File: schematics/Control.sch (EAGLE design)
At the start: 57 parts, among them IC1 THAT1646, IC2 THAT1646, IC5 NE5532N

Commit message: rev01 for pcbtrain express fab
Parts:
- removed BOOT, BOOT1, JP4: (no value), SparkFun:M03PTH
- removed C501, C502: 2n7 C0G, Rebel:C-EUC0603
- removed C503, C504: 100n, Rebel:C-EUC0603
- removed JP2: (no value), SparkFun:M02PTH
- added C10, C300, C301, C9: 0.1uF, capacitor-wima:C5/3.5
- added C11, C12, C610: 100n, rcl:C-EU050-025X075
- added C13, C14: 2n7 C0G, rcl:C-EU050-025X075
- added C15, C16, C611: 100uF, rcl:CPOL-EUE2.5-7
- added IN2: (no value), SparkFun:M02PTH
- added J4, J5: NEUTRIK_NMJ6HCD2, neutrik_jacks:NEUTRIK_NMJ6HCD2
- added JP13: (no value), SparkFun:M05PTH
- added R1, R2, R3, R4, R5: 91R, Rebel:R-EU_0204/7
- added R300, R301: 2M, Rebel:R-EU_0204/7
- added UART: (no value), SparkFun:M03PTH
- JP1: device SparkFun:M02PTH -> SparkFun:M05PTH
- R501, R502, R503, R504, R505, R506, R507, R508, R509, R510: device Rebel:R-EU_0603 -> Rebel:R-EU_0204/7
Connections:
- removed net +3V3: BOOT.3, BOOT1.3, JP3.3, JP4.3, JP5.3
- removed net AINA: C501.1, R503.2
- removed net AINB: C502.1, R508.2
- removed net BOOT0: BOOT.2, BOOT1.2, JP12.2, JP9.2
- removed net INL: R502.1
- removed net INR: R507.1
- removed net L_IN1: IN.1
- removed net L_IN2: IN1.1
- removed net L_OUT1: HP.2
- removed net L_OUT2: HP1.2
- removed net OUT_LEFT: IC1.4
- removed net OUT_RIGHT: IC2.4
- removed net R_IN1: IN.2
- removed net R_IN2: IN1.2
- removed net R_OUT1: HP.1
- removed net R_OUT2: HP1.1
- removed net USB_VBUS: JP1.2, JP2.2, USB.4, USB1.4
- new net ADC1_A: ADC.4
- new net ADC2_A: ADC.3
- new net ADC3_A: ADC.2
- new net ADC4_A: ADC.1
- new net FX_IN_L: C300.2, J4.T, J5.TN, R300.2
- new net FX_IN_R: C301.2, J5.T, R301.2
- new net L_IN_A: IN.1, R1.1
- new net L_IN_B: C13.1, IN1.1, R503.2
- new net L_OUT_A: C10.2, HP.2
- new net L_OUT_B: HP1.2, R1.2
- new net N$26: C300.1, R502.1
- new net N$30: C301.1, R507.1
- new net N$7: C9.1, IC2.4
- new net N$9: C10.1, IC1.4
- new net PA2_A: JP7.2
- new net PA3_A: JP7.1
- new net PB6_A: JP9.4
- new net PB7_A: JP9.3
- new net PE2_A: JP10.4
- new net PE3_A: JP10.3
- new net PE4_A: JP10.2
- new net PE5_A: JP10.1
- new net PG14_A: JP9.1
- new net RX: R3.1, UART.3
- new net RX_A: JP13.2, R5.1
- new net RX_B: JP1.2, R3.2
- new net R_IN_A: IN.2, R2.1
- new net R_IN_B: C14.1, IN1.2, R508.2
- new net R_OUT_A: C9.2, HP.1
- new net R_OUT_B: HP1.1, R2.2
- new net TX: R4.1, UART.1
- new net TX_A: JP13.3, R4.2
- new net TX_B: JP1.3, R5.2
- new net USB_DM_A: USB.3
- new net USB_DP_A: USB.2
- new net USB_ID_A: USB.1
- net +12V: now also C11.1; no longer C503.1
- net +5V: now also C15.+, C16.+; no longer JP1.1, JP2.1, JP4.1
- net -12V: now also C12.1; no longer C504.1
- net ADC1: no longer ADC.4
- net ADC2: no longer ADC.3
- net ADC3: no longer ADC.2
- net ADC4: no longer ADC.1
- net CS_VREF: now also C13.2, C14.2, C610.1, C611.+, VMID1.1; no longer C501.2, C502.2
- net GND: now also C11.2, C12.2, C15.-, C16.-, C610.2, C611.-, IN2.2, J4.S, J4.TN, J5.S, JP12.2, JP9.2, R300.1, R301.1, UART.2; no longer BOOT.1, BOOT1.1, C503.2, C504.2, JP4.2
- net GNDA: now also IN2.1
- net PA2: no longer JP7.2
- net PA3: no longer JP7.1
- net PB6: no longer JP9.4
- net PB7: no longer JP9.3
- net PE2: no longer JP10.4
- net PE3: no longer JP10.3
- net PE4: no longer JP10.2
- net PE5: no longer JP10.1
- net PG14: no longer JP9.1
- net USB_DM: no longer USB.3
- net USB_DP: no longer USB.2
- net USB_ID: no longer USB.1
- net VCC/2: no longer VMID1.1
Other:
- note added: "Copyright 2016 Rebel Technology"
- note added: "OWL Rack Revision 1"
- note removed: "Copyright 2015 Rebel Technology"
- note removed: "OWL Modular Revision 2"
- moved on the sheet: C1, C2, C3, C4, C5, C6, C7, C8, IC1, IC2, LEFT, RIGHT

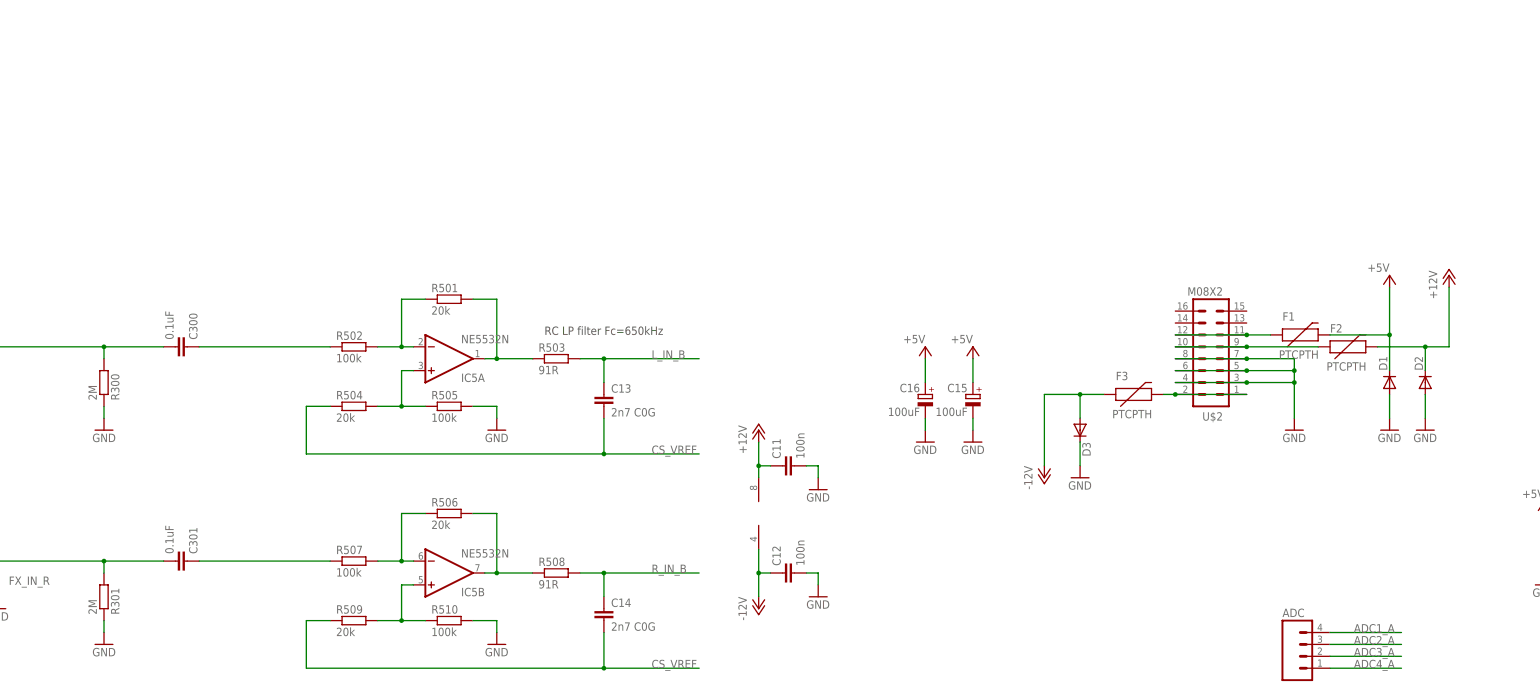
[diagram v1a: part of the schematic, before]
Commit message: added +5v reg, change power connection, reduced board size
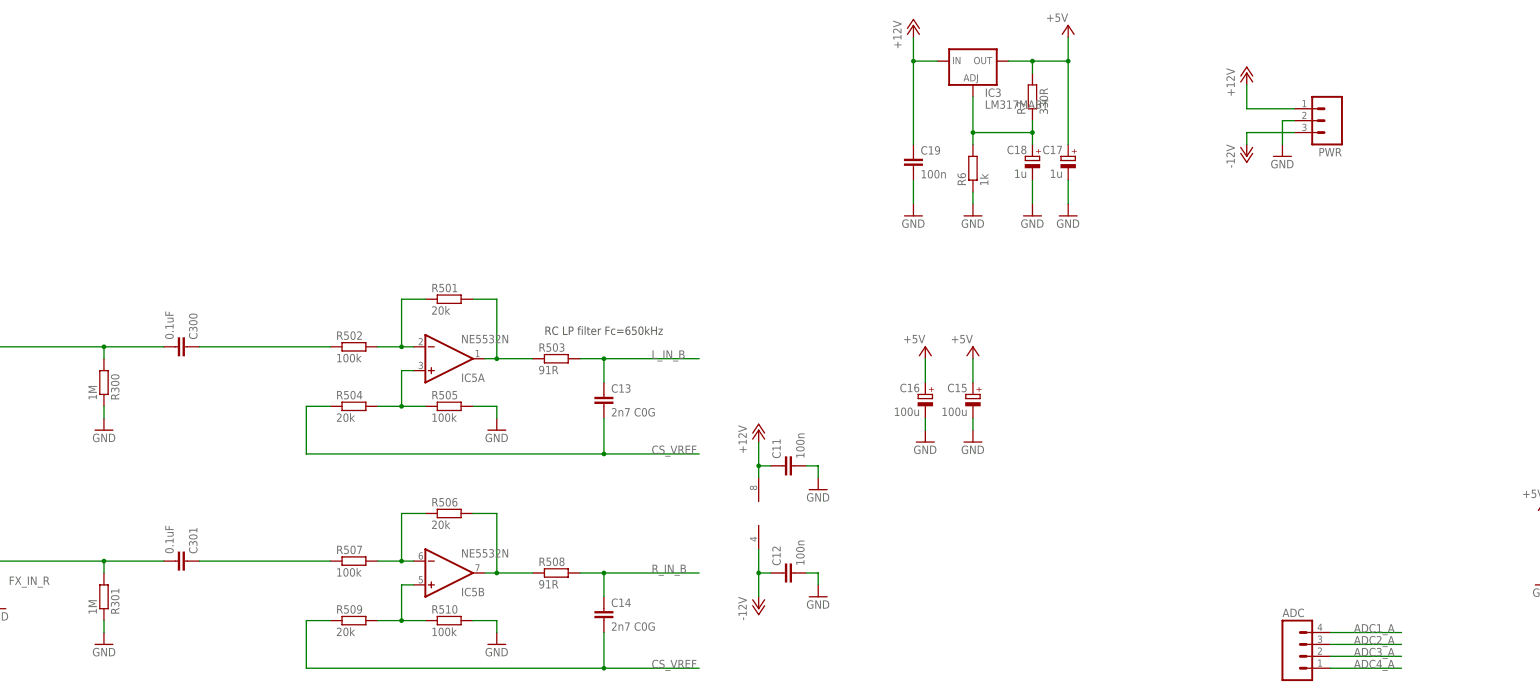
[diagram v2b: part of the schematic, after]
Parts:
- removed D1, D2, D3: (no value), Rebel:DIODE1N4001
- removed F1, F2, F3: PTCPTH, Rebel:PTCPTH
- removed U$2: M08X2, SparkFun:M08X2
- added C17, C18: 1u, rcl:CPOL-EUE2.5-7
- added C19: 100n, rcl:C-EU050-025X075
- added IC3: LM317MABT, v-reg:LM317MABT
- added PWR: (no value), SparkFun:M03PTH
- added R6: 1k, Rebel:R-EU_0204/7
- added R7: 330R, Rebel:R-EU_0204/7
- C15, C16: value 100uF -> 100u
- R300, R301: value 2M -> 1M
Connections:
- removed net N$44: F1.1, U$2.11, U$2.12
- removed net N$45: F2.1, U$2.10, U$2.9
- removed net N$6: F3.2, U$2.1, U$2.2
- new net N$11: C18.+, IC3.ADJ, R6.2, R7.1
- net +12V: now also C19.1, IC3.IN, PWR.1; no longer D2.C, F2.2
- net +5V: now also C17.+, IC3.OUT, R7.2; no longer D1.C, F1.2
- net -12V: now also PWR.3; no longer D3.A, F3.1
- net GND: now also C17.-, C18.-, C19.2, PWR.2, R6.1; no longer D1.A, D2.A, D3.C, U$2.3, U$2.4, U$2.5, U$2.6, U$2.7, U$2.8

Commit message: added usb connections and adjusted audio input circuit
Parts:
- added R8, R9: 1M, Rebel:R-EU_0204/7
- added USBA, USBB: (no value), SparkFun:M03PTH
- R501, R504, R506, R509: value 20k -> 10k
- R502, R505, R507, R510: value 100k -> 10k
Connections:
- net USB_ID renamed USB_ID_B
- removed net USB_DM: USB1.3
- removed net USB_DP: USB1.2
- new net USB_DM_B: USB1.3, USBB.3
- new net USB_DP_B: USB1.2, USBB.1
- net GND: now also R8.1, R9.1, USBA.2, USBB.2
- net N$26: now also R8.2
- net N$30: now also R9.2
- net USB_DM_A: now also USBA.3
- net USB_DP_A: now also USBA.1
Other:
- note added: "OWL Rack Revision 2"
- note removed: "OWL Rack Revision 1"
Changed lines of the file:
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@@
 <part name="P+6" library="supply1" deviceset="+12V" device=""/>
 <part name="P-1" library="supply1" deviceset="-12V" device=""/>
-<part name="R501" library="Rebel" deviceset="R-EU_" device="0204/7" value="20k"/>
-<part name="R504" library="Rebel" deviceset="R-EU_" device="0204/7" value="20k"/>
-<part name="R505" library="Rebel" deviceset="R-EU_" device="0204/7" value="100k"/>
-<part name="R502" library="Rebel" deviceset="R-EU_" device="0204/7" value="100k"/>
+<part name="R501" library="Rebel" deviceset="R-EU_" device="0204/7" value="10k"/>
+<part name="R504" library="Rebel" deviceset="R-EU_" device="0204/7" value="10k"/>
+<part name="R505" library="Rebel" deviceset="R-EU_" device="0204/7" value="10k"/>
+<part name="R502" library="Rebel" deviceset="R-EU_" device="0204/7" value="10k"/>
 <part name="GND2" library="supply1" deviceset="GND" device=""/>
-<part name="R506" library="Rebel" deviceset="R-EU_" device="0204/7" value="20k"/>
-<part name="R509" library="Rebel" deviceset="R-EU_" device="0204/7" value="20k"/>
-<part name="R510" library="Rebel" deviceset="R-EU_" device="0204/7" value="100k"/>
-<part name="R507" library="Rebel" deviceset="R-EU_" device="0204/7" value="100k"/>
+<part name="R506" library="Rebel" deviceset="R-EU_" device="0204/7" value="10k"/>
+<part name="R509" library="Rebel" deviceset="R-EU_" device="0204/7" value="10k"/>
+<part name="R510" library="Rebel" deviceset="R-EU_" device="0204/7" value="10k"/>
+<part name="R507" library="Rebel" deviceset="R-EU_" device="0204/7" value="10k"/>
 <part name="GND6" library="supply1" deviceset="GND" device=""/>
 <part name="IC5" library="linear" deviceset="NE5532" device="N" value="NE5532N"/>
@@
 <part name="C18" library="rcl" deviceset="CPOL-EU" device="E2.5-7" value="1u"/>
 <part name="GND5" library="supply1" deviceset="GND" device=""/>
+<part name="USBA" library="SparkFun" deviceset="M03" device="PTH"/>
+<part name="GND20" library="supply1" deviceset="GND" device=""/>
+<part name="USBB" library="SparkFun" deviceset="M03" device="PTH"/>
+<part name="GND31" library="supply1" deviceset="GND" device=""/>
+<part name="R8" library="Rebel" deviceset="R-EU_" device="0204/7" value="1M"/>
+<part name="GND32" library="supply1" deviceset="GND" device=""/>
+<part name="R9" library="Rebel" deviceset="R-EU_" device="0204/7" value="1M"/>
+<part name="GND34" library="supply1" deviceset="GND" device=""/>
 </parts>
 <sheets>
 <sheet>
 <plain>
-<text x="-25.4" y="-58.42" size="6.4516" layer="97" font="vector">OWL Rack Revision 1</text>
+<text x="-25.4" y="-58.42" size="6.4516" layer="97" font="vector">OWL Rack Revision 2</text>
 <text x="-25.4" y="-66.04" size="3.81" layer="97" font="vector">Copyright 2016 Rebel Technology</text>
 <text x="-25.4" y="-73.66" size="3.81" layer="97" font="vector">Published under the GNU GPL</text>
@@
 <instance part="C18" gate="G$1" x="88.9" y="157.48" rot="MR0"/>
 <instance part="GND5" gate="1" x="88.9" y="144.78"/>
+<instance part="USBA" gate="G$1" x="246.38" y="-35.56" rot="R180"/>
+<instance part="GND20" gate="1" x="236.22" y="-45.72"/>
+<instance part="USBB" gate="G$1" x="368.3" y="-38.1" rot="R180"/>
+<instance part="GND31" gate="1" x="358.14" y="-48.26"/>
+<instance part="R8" gate="G$1" x="-83.82" y="109.22" rot="MR90"/>
+<instance part="GND32" gate="1" x="-83.82" y="99.06" rot="MR0"/>
+<instance part="R9" gate="G$1" x="-83.82" y="63.5" rot="MR90"/>
+<instance part="GND34" gate="1" x="-83.82" y="53.34" rot="MR0"/>
 </instances>
 <busses>
@@
 <wire x1="88.9" y1="147.32" x2="88.9" y2="152.4" width="0.1524" layer="91"/>
 </segment>
+<segment>
+<pinref part="USBA" gate="G$1" pin="2"/>
+<pinref part="GND20" gate="1" pin="GND"/>
+<wire x1="238.76" y1="-35.56" x2="236.22" y2="-35.56" width="0.1524" layer="91"/>
+<wire x1="236.22" y1="-35.56" x2="236.22" y2="-43.18" width="0.1524" layer="91"/>
+</segment>
+<segment>
+<pinref part="USBB" gate="G$1" pin="2"/>
+<pinref part="GND31" gate="1" pin="GND"/>
+<wire x1="360.68" y1="-38.1" x2="358.14" y2="-38.1" width="0.1524" layer="91"/>
+<wire x1="358.14" y1="-38.1" x2="358.14" y2="-45.72" width="0.1524" layer="91"/>
+</segment>
+<segment>
+<pinref part="R8" gate="G$1" pin="1"/>
+<pinref part="GND32" gate="1" pin="GND"/>
+<wire x1="-83.82" y1="101.6" x2="-83.82" y2="104.14" width="0.1524" layer="91"/>
+</segment>
+<segment>
+<pinref part="R9" gate="G$1" pin="1"/>
+<pinref part="GND34" gate="1" pin="GND"/>
+<wire x1="-83.82" y1="55.88" x2="-83.82" y2="58.42" width="0.1524" layer="91"/>
+</segment>
 </net>
 <net name="+5V" class="0">
@@
 </segment>
 </net>
-<net name="USB_DM" class="0">
-<segment>
-<wire x1="304.8" y1="-38.1" x2="322.58" y2="-38.1" width="0.1524" layer="91"/>
-<label x="307.34" y="-38.1" size="1.778" layer="95"/>
-<pinref part="USB1" gate="G$1" pin="3"/>
-</segment>
-</net>
-<net name="USB_DP" class="0">
-<segment>
-<wire x1="304.8" y1="-35.56" x2="322.58" y2="-35.56" width="0.1524" layer="91"/>
-<label x="307.34" y="-35.56" size="1.778" layer="95"/>
-<pinref part="USB1" gate="G$1" pin="2"/>
-</segment>
-</net>
-<net name="USB_ID" class="0">
+<net name="USB_ID_B" class="0">
 <segment>
 <label x="307.34" y="-33.02" size="1.778" layer="95"/>
@@
 <pinref part="C300" gate="G$1" pin="1"/>
 <pinref part="R502" gate="G$1" pin="1"/>
-<wire x1="-88.9" y1="116.84" x2="-60.96" y2="116.84" width="0.1524" layer="91"/>
+<wire x1="-88.9" y1="116.84" x2="-83.82" y2="116.84" width="0.1524" layer="91"/>
+<pinref part="R8" gate="G$1" pin="2"/>
+<wire x1="-83.82" y1="116.84" x2="-60.96" y2="116.84" width="0.1524" layer="91"/>
+<wire x1="-83.82" y1="114.3" x2="-83.82" y2="116.84" width="0.1524" layer="91"/>
+<junction x="-83.82" y="116.84"/>
 </segment>
 </net>
@@
 <pinref part="C301" gate="G$1" pin="1"/>
 <pinref part="R507" gate="G$1" pin="1"/>
-<wire x1="-60.96" y1="71.12" x2="-88.9" y2="71.12" width="0.1524" layer="91"/>
+<wire x1="-60.96" y1="71.12" x2="-83.82" y2="71.12" width="0.1524" layer="91"/>
+<pinref part="R9" gate="G$1" pin="2"/>
+<wire x1="-83.82" y1="71.12" x2="-88.9" y2="71.12" width="0.1524" layer="91"/>
+<wire x1="-83.82" y1="68.58" x2="-83.82" y2="71.12" width="0.1524" layer="91"/>
+<junction x="-83.82" y="71.12"/>
 </segment>
 </net>
@@
 <pinref part="USB" gate="G$1" pin="2"/>
 </segment>
+<segment>
+<pinref part="USBA" gate="G$1" pin="1"/>
+<wire x1="238.76" y1="-33.02" x2="220.98" y2="-33.02" width="0.1524" layer="91"/>
+<label x="220.98" y="-33.02" size="1.778" layer="95"/>
+</segment>
 </net>
 <net name="USB_DM_A" class="0">
@@
 <label x="185.42" y="-35.56" size="1.778" layer="95"/>
 <pinref part="USB" gate="G$1" pin="3"/>
+</segment>
+<segment>
+<pinref part="USBA" gate="G$1" pin="3"/>
+<wire x1="238.76" y1="-38.1" x2="220.98" y2="-38.1" width="0.1524" layer="91"/>
+<label x="220.98" y="-38.1" size="1.778" layer="95"/>
 </segment>
 </net>
@@
 </segment>
 </net>
+<net name="USB_DP_B" class="0">
+<segment>
+<pinref part="USBB" gate="G$1" pin="1"/>
+<wire x1="360.68" y1="-35.56" x2="342.9" y2="-35.56" width="0.1524" layer="91"/>
+<label x="342.9" y="-35.56" size="1.778" layer="95"/>
+</segment>
+<segment>
+<wire x1="304.8" y1="-35.56" x2="322.58" y2="-35.56" width="0.1524" layer="91"/>
+<label x="307.34" y="-35.56" size="1.778" layer="95"/>
+<pinref part="USB1" gate="G$1" pin="2"/>
+</segment>
+</net>
+<net name="USB_DM_B" class="0">
+<segment>
+<pinref part="USBB" gate="G$1" pin="3"/>
+<wire x1="360.68" y1="-40.64" x2="342.9" y2="-40.64" width="0.1524" layer="91"/>
+<label x="342.9" y="-40.64" size="1.778" layer="95"/>
+</segment>
+<segment>
+<wire x1="304.8" y1="-38.1" x2="322.58" y2="-38.1" width="0.1524" layer="91"/>
+<label x="307.34" y="-38.1" size="1.778" layer="95"/>
+<pinref part="USB1" gate="G$1" pin="3"/>
+</segment>
+</net>
